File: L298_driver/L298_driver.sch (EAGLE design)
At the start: 23 parts, among them U1 L298

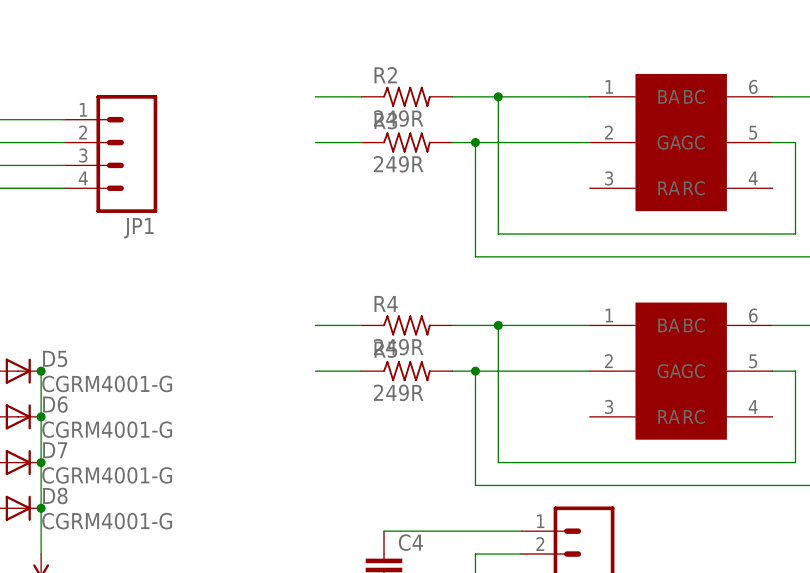
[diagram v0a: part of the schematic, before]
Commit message: Change resistor value for 3.3V operation.
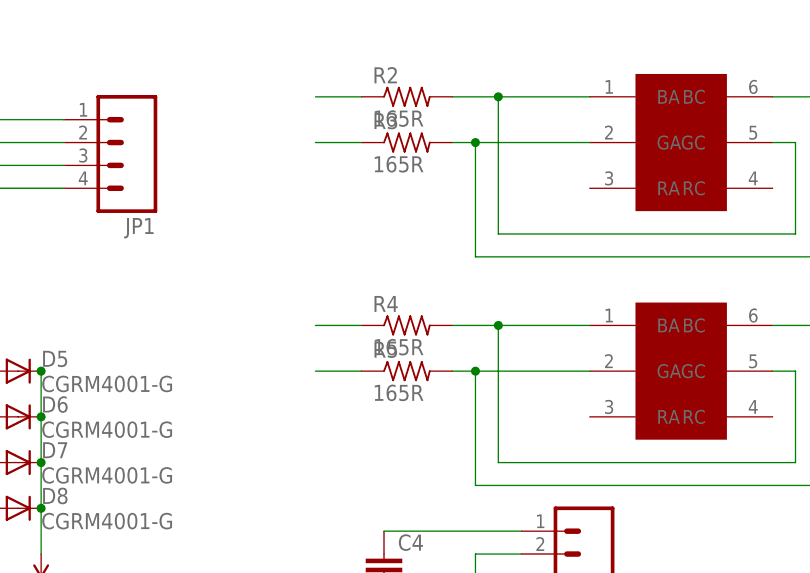
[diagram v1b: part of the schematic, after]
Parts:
- R2, R3, R4, R5: value 249R -> 165R
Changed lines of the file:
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@@
 <part name="U$2" library="SparkFun-Aesthetics" deviceset="5V" device=""/>
 <part name="P+1" library="SparkFun-Aesthetics" deviceset="VCC" device=""/>
-<part name="R2" library="resistor" deviceset="R-US_" device="R0402" value="249R"/>
+<part name="R2" library="resistor" deviceset="R-US_" device="R0402" value="165R"/>
 <part name="LED_A" library="yoos" deviceset="LRTB_R98G" device=""/>
 <part name="JP2" library="SparkFun-Connectors" deviceset="M03" device="-SCREW-5MM"/>
@@
 <part name="GND6" library="SparkFun-Aesthetics" deviceset="GND" device=""/>
 <part name="LED_B" library="yoos" deviceset="LRTB_R98G" device=""/>
-<part name="R3" library="resistor" deviceset="R-US_" device="R0402" value="249R"/>
-<part name="R4" library="resistor" deviceset="R-US_" device="R0402" value="249R"/>
-<part name="R5" library="resistor" deviceset="R-US_" device="R0402" value="249R"/>
+<part name="R3" library="resistor" deviceset="R-US_" device="R0402" value="165R"/>
+<part name="R4" library="resistor" deviceset="R-US_" device="R0402" value="165R"/>
+<part name="R5" library="resistor" deviceset="R-US_" device="R0402" value="165R"/>
 <part name="OUT_B" library="SparkFun-Connectors" deviceset="M02" device="5MM"/>
 <part name="D2" library="diode" deviceset="CGRM400*-G" device="" technology="1"/>

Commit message: Finish up.
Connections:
- net IN1: now also JP1.4; no longer JP1.1
- net IN2: now also JP1.3; no longer JP1.2
- net IN3: now also JP1.2; no longer JP1.3
- net IN4: now also JP1.1; no longer JP1.4
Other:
- moved on the sheet: JP1
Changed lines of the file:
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@@
 <instance part="C3" gate="G$1" x="137.16" y="55.88"/>
 <instance part="C1" gate="G$1" x="60.96" y="20.32"/>
-<instance part="JP1" gate="G$1" x="104.14" y="119.38" rot="R180"/>
+<instance part="JP1" gate="G$1" x="104.14" y="116.84" rot="MR0"/>
 </instances>
 <busses>
@@
 <segment>
 <pinref part="U1" gate="G$1" pin="IN1"/>
+<pinref part="JP1" gate="G$1" pin="4"/>
 <wire x1="73.66" y1="121.92" x2="99.06" y2="121.92" width="0.1524" layer="91"/>
-<pinref part="JP1" gate="G$1" pin="1"/>
 </segment>
 </net>
@@
 </segment>
 <segment>
+<pinref part="JP1" gate="G$1" pin="3"/>
 <pinref part="U1" gate="G$1" pin="IN2"/>
-<wire x1="73.66" y1="119.38" x2="99.06" y2="119.38" width="0.1524" layer="91"/>
-<pinref part="JP1" gate="G$1" pin="2"/>
+<wire x1="99.06" y1="119.38" x2="73.66" y2="119.38" width="0.1524" layer="91"/>
 </segment>
 </net>
@@
 <segment>
 <pinref part="U1" gate="G$1" pin="IN3"/>
+<pinref part="JP1" gate="G$1" pin="2"/>
 <wire x1="73.66" y1="116.84" x2="99.06" y2="116.84" width="0.1524" layer="91"/>
-<pinref part="JP1" gate="G$1" pin="3"/>
 </segment>
 </net>
@@
 </segment>
 <segment>
+<pinref part="JP1" gate="G$1" pin="1"/>
 <pinref part="U1" gate="G$1" pin="IN4"/>
-<wire x1="73.66" y1="114.3" x2="99.06" y2="114.3" width="0.1524" layer="91"/>
-<pinref part="JP1" gate="G$1" pin="4"/>
+<wire x1="99.06" y1="114.3" x2="73.66" y2="114.3" width="0.1524" layer="91"/>
 </segment>
 </net>
